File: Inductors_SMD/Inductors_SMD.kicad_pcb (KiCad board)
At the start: 2 copper layers, 11 parts

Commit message: Added new library with SMD inductors, mostly from Murata plus one of the most widespread sizes CDxx and DRxx.
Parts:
- removed CD104: VAL**, Inductors_SMD:CD104
- removed CD105: VAL**, Inductors_SMD:CD105
- removed CD32: VAL**, Inductors_SMD:CD32
- removed CD43: VAL**, Inductors_SMD:CD43
- removed CD54: VAL**, Inductors_SMD:CD54
- removed CD73: VAL**, Inductors_SMD:CD73
- removed CD75: VAL**, Inductors_SMD:CD75
- removed DR125: VAL**, Inductors_SMD:DR125
- removed DR127: VAL**, Inductors_SMD:DR127
- removed DR73: VAL**, Inductors_SMD:DR73
- removed DR74: VAL**, Inductors_SMD:DR74
- added REF**: CD104, CD104, F.Cu at (20.0, 20.0)
- added REF**: DR73, DR73, F.Cu at (34.0, 110.0)
- added REF**: LQM31P_Reflow, LQM31P, F.Cu at (132.0, 190.0)
- added REF**: LQM32P_Hand, LQM32P, F.Cu at (216.0, 20.0)
- added REF**: LQM32P_Reflow, LQM32P, F.Cu at (188.0, 20.0)
- added REF**: LQP02TN_Hand, LQP02TN, F.Cu at (216.0, 30.0)
- added REF**: LQP02TN_Reflow, LQP02TN, F.Cu at (188.0, 30.0)
- added REF**: LQP02TQ_Hand, LQP02TQ, F.Cu at (216.0, 40.0)
- added REF**: LQP02TQ_Reflow, LQP02TQ, F.Cu at (188.0, 40.0)
- added REF**: LQP03T_Hand, LQP03T, F.Cu at (216.0, 50.0)
- added REF**: LQP03T_Reflow, LQP03T, F.Cu at (188.0, 50.0)
- added REF**: LQP15M_Hand, LQP15M, F.Cu at (216.0, 60.0)
- added REF**: DR74, DR74, F.Cu at (20.0, 120.0)
- added REF**: LQP15M_Reflow, LQP15M, F.Cu at (188.0, 60.0)
- added REF**: LQP18M_Hand, LQP18M, F.Cu at (216.0, 70.0)
- added REF**: LQP18M_Reflow, LQP18M, F.Cu at (188.0, 70.0)
- added REF**: LQW03A_Hand, LQW03A, F.Cu at (216.0, 80.0)
- added REF**: LQW03A_Reflow, LQW03A, F.Cu at (188.0, 80.0)
- added REF**: LQW04A_Hand, LQW04A, F.Cu at (216.0, 90.0)
- added REF**: LQW04A_Reflow, LQW04A, F.Cu at (188.0, 90.0)
- added REF**: LQW15A_00_Hand, LQW15A_00, F.Cu at (216.0, 100.0)
- added REF**: LQW15A_00_Reflow, LQW15A_00, F.Cu at (188.0, 100.0)
- added REF**: LQW15A_80_Hand, LQW15A_80, F.Cu at (216.0, 110.0)
- added REF**: LQB15NN_Hand, LQB15NN, F.Cu at (48.0, 130.0)
- added REF**: LQW15A_80_Reflow, LQW15A_80, F.Cu at (188.0, 110.0)
- added REF**: LQW15C_00_Hand, LQW15C_00, F.Cu at (216.0, 120.0)
- added REF**: LQW15C_00_Reflow, LQW15C_00, F.Cu at (188.0, 120.0)
- added REF**: LQW15C_10_Hand, LQW15C_10, F.Cu at (216.0, 130.0)
- added REF**: LQW15C_10_Reflow, LQW15C_10, F.Cu at (188.0, 130.0)
- added REF**: LQW18A_00_Hand, LQW18A_00, F.Cu at (216.0, 140.0)
- added REF**: LQW18A_00_Reflow, LQW18A_00, F.Cu at (188.0, 140.0)
- added REF**: LQW18A_80_Hand, LQW18A_80, F.Cu at (216.0, 150.0)
- added REF**: LQW18A_80_Reflow, LQW18A_80, F.Cu at (188.0, 150.0)
- added REF**: LQW18C_Hand, LQW18C, F.Cu at (216.0, 160.0)
- added REF**: LQB15NN_Reflow, LQB15NN, F.Cu at (20.0, 130.0)
- added REF**: LQW18C_Reflow, LQW18C, F.Cu at (188.0, 160.0)
- added REF**: LQW21H_Hand, LQW21H, F.Cu at (216.0, 170.0)
- added REF**: LQW21H_Reflow, LQW21H, F.Cu at (188.0, 170.0)
- added REF**: LQW2BA_Hand, LQW2BA, F.Cu at (216.0, 180.0)
- added REF**: LQW2BA_Reflow, LQW2BA, F.Cu at (188.0, 180.0)
- added REF**: LQW2BH_Hand, LQW2BH, F.Cu at (216.0, 190.0)
- added REF**: LQW2BH_Reflow, LQW2BH, F.Cu at (188.0, 190.0)
- added REF**: LQW2UA_Hand, LQW2UA, F.Cu at (272.0, 20.0)
- added REF**: LQW2UA_Reflow, LQW2UA, F.Cu at (244.0, 20.0)
- added REF**: LQW31H_Hand, LQW31H, F.Cu at (272.0, 30.0)
- added REF**: LQB18N_Flow, LQB18N, F.Cu at (34.0, 140.0)
- added REF**: LQW31H_Reflow, LQW31H, F.Cu at (244.0, 30.0)
- added REF**: LQB18N_Hand, LQB18N, F.Cu at (48.0, 140.0)
- added REF**: LQB18N_Reflow, LQB18N, F.Cu at (20.0, 140.0)
- added REF**: LQG15H_Hand, LQG15H, F.Cu at (48.0, 150.0)
- added REF**: LQG15H_Reflow, LQG15H, F.Cu at (20.0, 150.0)
- added REF**: LQG18H_Hand, LQG18H, F.Cu at (48.0, 160.0)
- added REF**: CD105, CD105, F.Cu at (34.0, 30.0)
- added REF**: LQG18H_Reflow, LQG18H, F.Cu at (20.0, 160.0)
- added REF**: LQH2HP_GR_Hand, LQH2HP_GR, F.Cu at (48.0, 170.0)
- added REF**: LQH2HP_GR_Reflow, LQH2HP_GR, F.Cu at (20.0, 170.0)
- added REF**: LQH2HP_Hand, LQH2HP, F.Cu at (48.0, 180.0)
- added REF**: LQH2HP_Reflow, LQH2HP, F.Cu at (20.0, 180.0)
- added REF**: LQH2MC_Hand, LQH2MC, F.Cu at (48.0, 190.0)
- added REF**: LQH2MC_Reflow, LQH2MC, F.Cu at (20.0, 190.0)
- added REF**: LQH31C_Hand, LQH31C, F.Cu at (104.0, 20.0)
- added REF**: LQH31C_Reflow, LQH31C, F.Cu at (76.0, 20.0)
- added REF**: LQH31H_Hand, LQH31H, F.Cu at (104.0, 30.0)
- added REF**: CD32, CD32, F.Cu at (20.0, 40.0)
- added REF**: LQH31H_Reflow, LQH31H, F.Cu at (76.0, 30.0)
- added REF**: LQH31M_Hand, LQH31M, F.Cu at (104.0, 40.0)
- added REF**: LQH31M_Reflow, LQH31M, F.Cu at (76.0, 40.0)
- added REF**: LQH32C_Hand, LQH32C, F.Cu at (104.0, 50.0)
- added REF**: LQH32C_Reflow, LQH32C, F.Cu at (76.0, 50.0)
- added REF**: LQH32M_Hand, LQH32M, F.Cu at (104.0, 60.0)
- added REF**: LQH32M_Reflow, LQH32M, F.Cu at (76.0, 60.0)
- added REF**: LQH32P_Hand, LQH32P, F.Cu at (104.0, 70.0)
- added REF**: LQH32P_Reflow, LQH32P, F.Cu at (76.0, 70.0)
- added REF**: LQH3N_Hand, LQH3N, F.Cu at (104.0, 80.0)
- added REF**: CD43, CD43, F.Cu at (34.0, 50.0)
- added REF**: LQH3N_Reflow, LQH3N, F.Cu at (76.0, 80.0)
- added REF**: LQH43C_Hand, LQH43C, F.Cu at (104.0, 90.0)
- added REF**: LQH43C_Reflow, LQH43C, F.Cu at (76.0, 90.0)
- added REF**: LQH43M_Hand, LQH43M, F.Cu at (104.0, 100.0)
- added REF**: LQH43M_Reflow, LQH43M, F.Cu at (76.0, 100.0)
- added REF**: LQH43N_Hand, LQH43N, F.Cu at (104.0, 110.0)
- added REF**: LQH43N_Reflow, LQH43N, F.Cu at (76.0, 110.0)
- added REF**: LQH43P_Hand, LQH43P, F.Cu at (104.0, 120.0)
- added REF**: LQH43P_Reflow, LQH43P, F.Cu at (76.0, 120.0)
- added REF**: LQH44N_Hand, LQH44N, F.Cu at (104.0, 130.0)
- added REF**: CD54, CD54, F.Cu at (20.0, 60.0)
- added REF**: LQH44N_Reflow, LQH44N, F.Cu at (76.0, 130.0)
- added REF**: LQH44P_Hand, LQH44P, F.Cu at (104.0, 140.0)
- added REF**: LQH44P_Reflow, LQH44P, F.Cu at (76.0, 140.0)
- added REF**: LQH55D_Hand, LQH55D, F.Cu at (104.0, 150.0)
- added REF**: LQH55D_Reflow, LQH55D, F.Cu at (76.0, 150.0)
- added REF**: LQH5BP_Hand, LQH5BP, F.Cu at (104.0, 160.0)
- added REF**: LQH5BP_Reflow, LQH5BP, F.Cu at (76.0, 160.0)
- added REF**: LQH66S_Hand, LQH66S, F.Cu at (104.0, 170.0)
- added REF**: LQH66S_Reflow, LQH66S, F.Cu at (76.0, 170.0)
- added REF**: LQM18F_Flow, LQM18F, F.Cu at (90.0, 180.0)
- added REF**: CD73, CD73, F.Cu at (34.0, 70.0)
- added REF**: LQM18F_Hand, LQM18F, F.Cu at (104.0, 180.0)
- added REF**: LQM18F_Reflow, LQM18F, F.Cu at (76.0, 180.0)
- added REF**: LQM18N_Flow, LQM18N, F.Cu at (90.0, 190.0)
- added REF**: LQM18N_Hand, LQM18N, F.Cu at (104.0, 190.0)
- added REF**: LQM18N_Reflow, LQM18N, F.Cu at (76.0, 190.0)
- added REF**: LQM18P_Flow, LQM18P, F.Cu at (146.0, 20.0)
- added REF**: LQM18P_Hand, LQM18P, F.Cu at (160.0, 20.0)
- added REF**: LQM18P_Reflow, LQM18P, F.Cu at (132.0, 20.0)
- added REF**: LQM21D_Hand, LQM21D, F.Cu at (160.0, 30.0)
- added REF**: LQM21D_Reflow, LQM21D, F.Cu at (132.0, 30.0)
- added REF**: CD75, CD75, F.Cu at (20.0, 80.0)
- added REF**: LQM21F_Hand, LQM21F, F.Cu at (160.0, 40.0)
- added REF**: LQM21F_Reflow, LQM21F, F.Cu at (132.0, 40.0)
- added REF**: LQM21N_Flow, LQM21N, F.Cu at (146.0, 50.0)
- added REF**: LQM21N_Hand, LQM21N, F.Cu at (160.0, 50.0)
- added REF**: LQM21N_Reflow, LQM21N, F.Cu at (132.0, 50.0)
- added REF**: LQM21P_Hand, LQM21P, F.Cu at (160.0, 60.0)
- added REF**: LQM21P_Reflow, LQM21P, F.Cu at (132.0, 60.0)
- added REF**: LQM2HP_GH_1.5A_Hand, LQM2HP_GH_1.5A, F.Cu at (160.0, 70.0)
- added REF**: LQM2HP_GH_1.5A_Reflow, LQM2HP_GH_1.5A, F.Cu at (132.0, 70.0)
- added REF**: LQM2HP_GH_2.6A_Hand, LQM2HP_GH_2.6A, F.Cu at (160.0, 80.0)
- added REF**: DR125, DR125, F.Cu at (34.0, 90.0)
- added REF**: LQM2HP_GH_2.6A_Reflow, LQM2HP_GH_2.6A, F.Cu at (132.0, 80.0)
- added REF**: LQM2HP_GH_3.3A_Hand, LQM2HP_GH_3.3A, F.Cu at (160.0, 90.0)
- added REF**: LQM2HP_GH_3.3A_Reflow, LQM2HP_GH_3.3A, F.Cu at (132.0, 90.0)
- added REF**: LQM2HP_Hand, LQM2HP, F.Cu at (160.0, 100.0)
- added REF**: LQM2HP_JH_1.6A_Hand, LQM2HP_JH_1.6A, F.Cu at (160.0, 110.0)
- added REF**: LQM2HP_JH_1.6A_Reflow, LQM2HP_JH_1.6A, F.Cu at (132.0, 110.0)
- added REF**: LQM2HP_JH_2.4A_Hand, LQM2HP_JH_2.4A, F.Cu at (160.0, 120.0)
- added REF**: LQM2HP_JH_2.4A_Reflow, LQM2HP_JH_2.4A, F.Cu at (132.0, 120.0)
- added REF**: LQM2HP_JH_3.5A_Hand, LQM2HP_JH_3.5A, F.Cu at (160.0, 130.0)
- added REF**: LQM2HP_JH_3.5A_Reflow, LQM2HP_JH_3.5A, F.Cu at (132.0, 130.0)
- added REF**: DR127, DR127, F.Cu at (20.0, 100.0)
- added REF**: LQM2HP_Reflow, LQM2HP, F.Cu at (132.0, 140.0)
- added REF**: LQM2MP_GH_1.5A_Hand, LQM2MP_GH_1.5A, F.Cu at (160.0, 150.0)
- added REF**: LQM2MP_GH_1.5A_Reflow, LQM2MP_GH_1.5A, F.Cu at (132.0, 150.0)
- added REF**: LQM2MP_GH_2.5A_Hand, LQM2MP_GH_2.5A, F.Cu at (160.0, 160.0)
- added REF**: LQM2MP_GH_2.5A_Reflow, LQM2MP_GH_2.5A, F.Cu at (132.0, 160.0)
- added REF**: LQM2MP_GH_5A_Hand, LQM2MP_GH_5A, F.Cu at (160.0, 170.0)
- added REF**: LQM2MP_GH_5A_Reflow, LQM2MP_GH_5A, F.Cu at (132.0, 170.0)
- added REF**: LQM2MP_Hand, LQM2MP, F.Cu at (160.0, 180.0)
- added REF**: LQM2MP_Reflow, LQM2MP, F.Cu at (132.0, 180.0)
- added REF**: LQM31P_Hand, LQM31P, F.Cu at (160.0, 190.0)
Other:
- net class Default: clearance 0.254 -> 0.25; trace_width 0.254 -> 0.25; via_dia 0.889 -> 0.6; via_drill 0.635 -> 0.4
- rule trace_clearance: 0.254 -> 0.25
- rule trace_min: 0.254 -> 0.2
- rule via_min_drill: 0.508 -> 0.3
- rule via_min_size: 0.889 -> 0.4

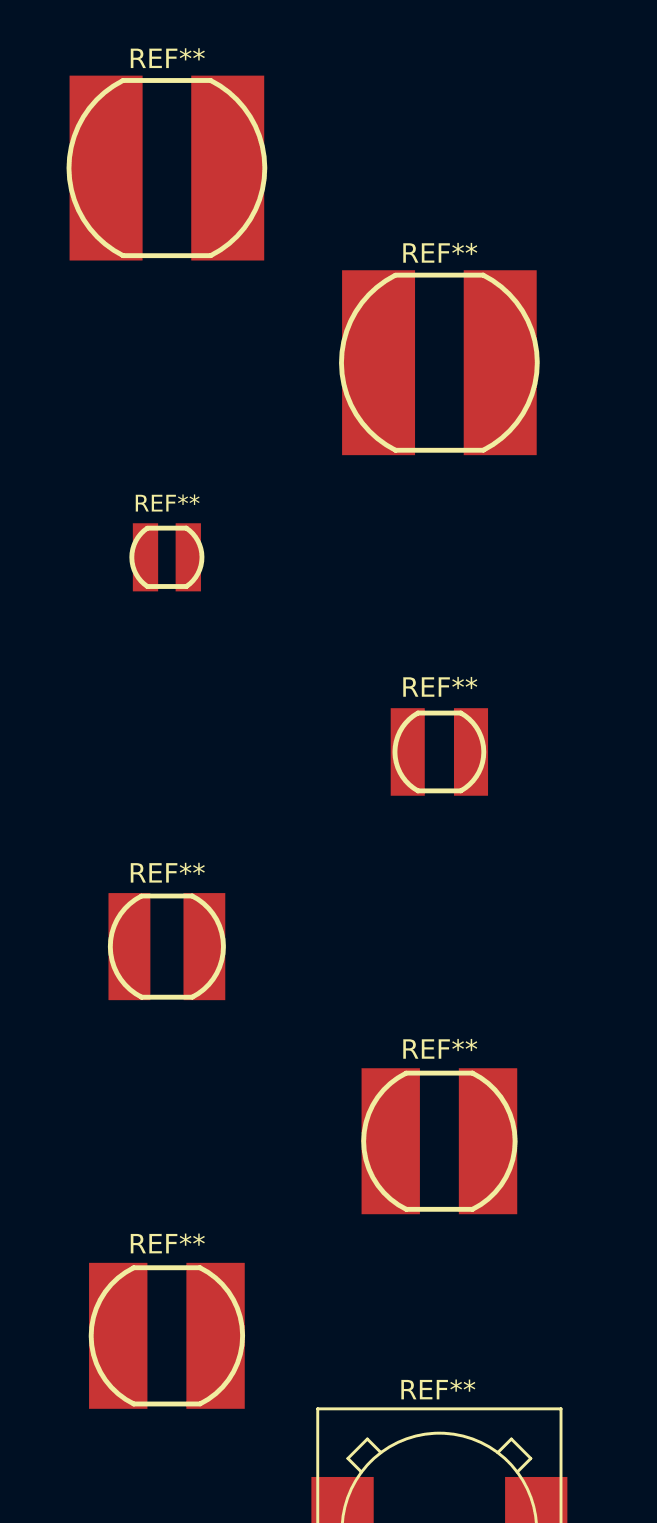
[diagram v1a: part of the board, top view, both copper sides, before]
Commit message: * Added Blender files to repository. * Fixed component generation scripts to avoid breaking some KLC rules
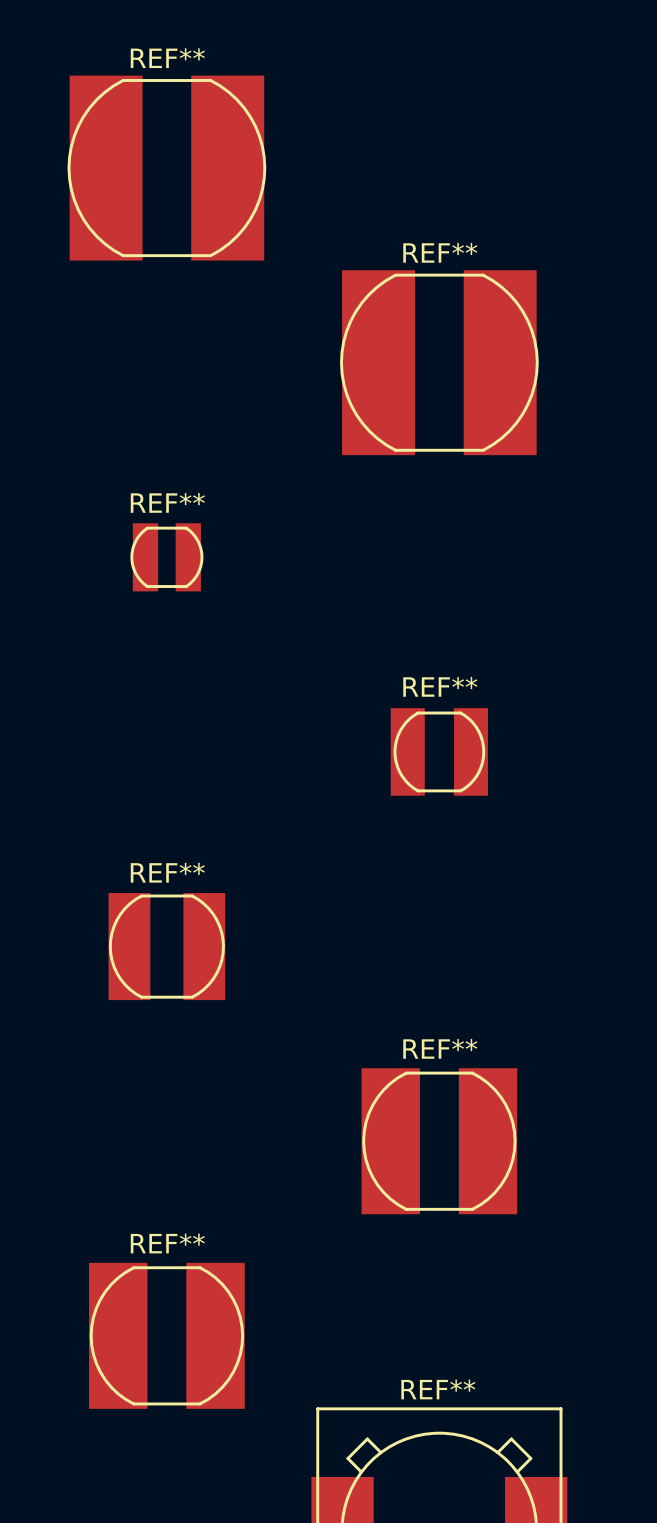
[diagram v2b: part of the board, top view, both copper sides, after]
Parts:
- removed the REF** at (132.0, 190.0)
- removed the REF** at (216.0, 20.0)
- removed the REF** at (188.0, 20.0)
- removed the REF** at (216.0, 30.0)
- removed the REF** at (188.0, 30.0)
- removed the REF** at (216.0, 40.0)
- removed the REF** at (188.0, 40.0)
- removed the REF** at (216.0, 50.0)
- removed the REF** at (188.0, 50.0)
- removed the REF** at (216.0, 60.0)
- removed the REF** at (188.0, 60.0)
- removed the REF** at (216.0, 70.0)
- removed the REF** at (188.0, 70.0)
- removed the REF** at (216.0, 80.0)
- removed the REF** at (188.0, 80.0)
- removed the REF** at (216.0, 90.0)
- removed the REF** at (188.0, 90.0)
- removed the REF** at (216.0, 100.0)
- removed the REF** at (188.0, 100.0)
- removed the REF** at (216.0, 110.0)
- removed the REF** at (48.0, 130.0)
- removed the REF** at (188.0, 110.0)
- removed the REF** at (216.0, 120.0)
- removed the REF** at (188.0, 120.0)
- removed the REF** at (216.0, 130.0)
- removed the REF** at (188.0, 130.0)
- removed the REF** at (216.0, 140.0)
- removed the REF** at (188.0, 140.0)
- removed the REF** at (216.0, 150.0)
- removed the REF** at (188.0, 150.0)
- removed the REF** at (216.0, 160.0)
- removed the REF** at (20.0, 130.0)
- removed the REF** at (188.0, 160.0)
- removed the REF** at (216.0, 170.0)
- removed the REF** at (188.0, 170.0)
- removed the REF** at (216.0, 180.0)
- removed the REF** at (188.0, 180.0)
- removed the REF** at (216.0, 190.0)
- removed the REF** at (188.0, 190.0)
- removed the REF** at (272.0, 20.0)
- removed the REF** at (244.0, 20.0)
- removed the REF** at (272.0, 30.0)
- removed the REF** at (34.0, 140.0)
- removed the REF** at (244.0, 30.0)
- removed the REF** at (48.0, 140.0)
- removed the REF** at (20.0, 140.0)
- removed the REF** at (48.0, 150.0)
- removed the REF** at (20.0, 150.0)
- removed the REF** at (48.0, 160.0)
- removed the REF** at (20.0, 160.0)
- removed the REF** at (48.0, 170.0)
- removed the REF** at (20.0, 170.0)
- removed the REF** at (48.0, 180.0)
- removed the REF** at (20.0, 180.0)
- removed the REF** at (48.0, 190.0)
- removed the REF** at (20.0, 190.0)
- removed the REF** at (104.0, 20.0)
- removed the REF** at (76.0, 20.0)
- removed the REF** at (104.0, 30.0)
- removed the REF** at (76.0, 30.0)
- removed the REF** at (104.0, 40.0)
- removed the REF** at (76.0, 40.0)
- removed the REF** at (104.0, 50.0)
- removed the REF** at (76.0, 50.0)
- removed the REF** at (104.0, 60.0)
- removed the REF** at (76.0, 60.0)
- removed the REF** at (104.0, 70.0)
- removed the REF** at (76.0, 70.0)
- removed the REF** at (104.0, 80.0)
- removed the REF** at (76.0, 80.0)
- removed the REF** at (104.0, 90.0)
- removed the REF** at (76.0, 90.0)
- removed the REF** at (104.0, 100.0)
- removed the REF** at (76.0, 100.0)
- removed the REF** at (104.0, 110.0)
- removed the REF** at (76.0, 110.0)
- removed the REF** at (104.0, 120.0)
- removed the REF** at (76.0, 120.0)
- removed the REF** at (104.0, 130.0)
- removed the REF** at (76.0, 130.0)
- removed the REF** at (104.0, 140.0)
- removed the REF** at (76.0, 140.0)
- removed the REF** at (104.0, 150.0)
- removed the REF** at (76.0, 150.0)
- removed the REF** at (104.0, 160.0)
- removed the REF** at (76.0, 160.0)
- removed the REF** at (104.0, 170.0)
- removed the REF** at (76.0, 170.0)
- removed the REF** at (90.0, 180.0)
- removed the REF** at (104.0, 180.0)
- removed the REF** at (76.0, 180.0)
- removed the REF** at (90.0, 190.0)
- removed the REF** at (104.0, 190.0)
- removed the REF** at (76.0, 190.0)
- removed the REF** at (146.0, 20.0)
- removed the REF** at (160.0, 20.0)
- removed the REF** at (132.0, 20.0)
- removed the REF** at (160.0, 30.0)
- removed the REF** at (132.0, 30.0)
- removed the REF** at (160.0, 40.0)
- removed the REF** at (132.0, 40.0)
- removed the REF** at (146.0, 50.0)
- removed the REF** at (160.0, 50.0)
- removed the REF** at (132.0, 50.0)
- removed the REF** at (160.0, 60.0)
- removed the REF** at (132.0, 60.0)
- removed the REF** at (160.0, 70.0)
- removed the REF** at (132.0, 70.0)
- removed the REF** at (160.0, 80.0)
- removed the REF** at (132.0, 80.0)
- removed the REF** at (160.0, 90.0)
- removed the REF** at (132.0, 90.0)
- removed the REF** at (160.0, 100.0)
- removed the REF** at (160.0, 110.0)
- removed the REF** at (132.0, 110.0)
- removed the REF** at (160.0, 120.0)
- removed the REF** at (132.0, 120.0)
- removed the REF** at (160.0, 130.0)
- removed the REF** at (132.0, 130.0)
- removed the REF** at (132.0, 140.0)
- removed the REF** at (160.0, 150.0)
- removed the REF** at (132.0, 150.0)
- removed the REF** at (160.0, 160.0)
- removed the REF** at (132.0, 160.0)
- removed the REF** at (160.0, 170.0)
- removed the REF** at (132.0, 170.0)
- removed the REF** at (160.0, 180.0)
- removed the REF** at (132.0, 180.0)
- removed the REF** at (160.0, 190.0)
- added REF**: LQM31P_Reflow, LQM31P_Reflow, F.Cu at (132.0, 190.0)
- added REF**: LQM32P_Hand, LQM32P_Hand, F.Cu at (216.0, 20.0)
- added REF**: LQM32P_Reflow, LQM32P_Reflow, F.Cu at (188.0, 20.0)
- added REF**: LQP02TN_Hand, LQP02TN_Hand, F.Cu at (216.0, 30.0)
- added REF**: LQP02TN_Reflow, LQP02TN_Reflow, F.Cu at (188.0, 30.0)
- added REF**: LQP02TQ_Hand, LQP02TQ_Hand, F.Cu at (216.0, 40.0)
- added REF**: LQP02TQ_Reflow, LQP02TQ_Reflow, F.Cu at (188.0, 40.0)
- added REF**: LQP03T_Hand, LQP03T_Hand, F.Cu at (216.0, 50.0)
- added REF**: LQP03T_Reflow, LQP03T_Reflow, F.Cu at (188.0, 50.0)
- added REF**: LQP15M_Hand, LQP15M_Hand, F.Cu at (216.0, 60.0)
- added REF**: LQP15M_Reflow, LQP15M_Reflow, F.Cu at (188.0, 60.0)
- added REF**: LQP18M_Hand, LQP18M_Hand, F.Cu at (216.0, 70.0)
- added REF**: LQP18M_Reflow, LQP18M_Reflow, F.Cu at (188.0, 70.0)
- added REF**: LQW03A_Hand, LQW03A_Hand, F.Cu at (216.0, 80.0)
- added REF**: LQW03A_Reflow, LQW03A_Reflow, F.Cu at (188.0, 80.0)
- added REF**: LQW04A_Hand, LQW04A_Hand, F.Cu at (216.0, 90.0)
- added REF**: LQW04A_Reflow, LQW04A_Reflow, F.Cu at (188.0, 90.0)
- added REF**: LQW15A_00_Hand, LQW15A_00_Hand, F.Cu at (216.0, 100.0)
- added REF**: LQW15A_00_Reflow, LQW15A_00_Reflow, F.Cu at (188.0, 100.0)
- added REF**: LQW15A_80_Hand, LQW15A_80_Hand, F.Cu at (216.0, 110.0)
- added REF**: LQB15NN_Hand, LQB15NN_Hand, F.Cu at (48.0, 130.0)
- added REF**: LQW15A_80_Reflow, LQW15A_80_Reflow, F.Cu at (188.0, 110.0)
- added REF**: LQW15C_00_Hand, LQW15C_00_Hand, F.Cu at (216.0, 120.0)
- added REF**: LQW15C_00_Reflow, LQW15C_00_Reflow, F.Cu at (188.0, 120.0)
- added REF**: LQW15C_10_Hand, LQW15C_10_Hand, F.Cu at (216.0, 130.0)
- added REF**: LQW15C_10_Reflow, LQW15C_10_Reflow, F.Cu at (188.0, 130.0)
- added REF**: LQW18A_00_Hand, LQW18A_00_Hand, F.Cu at (216.0, 140.0)
- added REF**: LQW18A_00_Reflow, LQW18A_00_Reflow, F.Cu at (188.0, 140.0)
- added REF**: LQW18A_80_Hand, LQW18A_80_Hand, F.Cu at (216.0, 150.0)
- added REF**: LQW18A_80_Reflow, LQW18A_80_Reflow, F.Cu at (188.0, 150.0)
- added REF**: LQW18C_Hand, LQW18C_Hand, F.Cu at (216.0, 160.0)
- added REF**: LQB15NN_Reflow, LQB15NN_Reflow, F.Cu at (20.0, 130.0)
- added REF**: LQW18C_Reflow, LQW18C_Reflow, F.Cu at (188.0, 160.0)
- added REF**: LQW21H_Hand, LQW21H_Hand, F.Cu at (216.0, 170.0)
- added REF**: LQW21H_Reflow, LQW21H_Reflow, F.Cu at (188.0, 170.0)
- added REF**: LQW2BA_Hand, LQW2BA_Hand, F.Cu at (216.0, 180.0)
- added REF**: LQW2BA_Reflow, LQW2BA_Reflow, F.Cu at (188.0, 180.0)
- added REF**: LQW2BH_Hand, LQW2BH_Hand, F.Cu at (216.0, 190.0)
- added REF**: LQW2BH_Reflow, LQW2BH_Reflow, F.Cu at (188.0, 190.0)
- added REF**: LQW2UA_Hand, LQW2UA_Hand, F.Cu at (272.0, 20.0)
- added REF**: LQW2UA_Reflow, LQW2UA_Reflow, F.Cu at (244.0, 20.0)
- added REF**: LQW31H_Hand, LQW31H_Hand, F.Cu at (272.0, 30.0)
- added REF**: LQB18N_Flow, LQB18N_Flow, F.Cu at (34.0, 140.0)
- added REF**: LQW31H_Reflow, LQW31H_Reflow, F.Cu at (244.0, 30.0)
- added REF**: LQB18N_Hand, LQB18N_Hand, F.Cu at (48.0, 140.0)
- added REF**: LQB18N_Reflow, LQB18N_Reflow, F.Cu at (20.0, 140.0)
- added REF**: LQG15H_Hand, LQG15H_Hand, F.Cu at (48.0, 150.0)
- added REF**: LQG15H_Reflow, LQG15H_Reflow, F.Cu at (20.0, 150.0)
- added REF**: LQG18H_Hand, LQG18H_Hand, F.Cu at (48.0, 160.0)
- added REF**: LQG18H_Reflow, LQG18H_Reflow, F.Cu at (20.0, 160.0)
- added REF**: LQH2HP_GR_Hand, LQH2HP_GR_Hand, F.Cu at (48.0, 170.0)
- added REF**: LQH2HP_GR_Reflow, LQH2HP_GR_Reflow, F.Cu at (20.0, 170.0)
- added REF**: LQH2HP_Hand, LQH2HP_Hand, F.Cu at (48.0, 180.0)
- added REF**: LQH2HP_Reflow, LQH2HP_Reflow, F.Cu at (20.0, 180.0)
- added REF**: LQH2MC_Hand, LQH2MC_Hand, F.Cu at (48.0, 190.0)
- added REF**: LQH2MC_Reflow, LQH2MC_Reflow, F.Cu at (20.0, 190.0)
- added REF**: LQH31C_Hand, LQH31C_Hand, F.Cu at (104.0, 20.0)
- added REF**: LQH31C_Reflow, LQH31C_Reflow, F.Cu at (76.0, 20.0)
- added REF**: LQH31H_Hand, LQH31H_Hand, F.Cu at (104.0, 30.0)
- added REF**: LQH31H_Reflow, LQH31H_Reflow, F.Cu at (76.0, 30.0)
- added REF**: LQH31M_Hand, LQH31M_Hand, F.Cu at (104.0, 40.0)
- added REF**: LQH31M_Reflow, LQH31M_Reflow, F.Cu at (76.0, 40.0)
- added REF**: LQH32C_Hand, LQH32C_Hand, F.Cu at (104.0, 50.0)
- added REF**: LQH32C_Reflow, LQH32C_Reflow, F.Cu at (76.0, 50.0)
- added REF**: LQH32M_Hand, LQH32M_Hand, F.Cu at (104.0, 60.0)
- added REF**: LQH32M_Reflow, LQH32M_Reflow, F.Cu at (76.0, 60.0)
- added REF**: LQH32P_Hand, LQH32P_Hand, F.Cu at (104.0, 70.0)
- added REF**: LQH32P_Reflow, LQH32P_Reflow, F.Cu at (76.0, 70.0)
- added REF**: LQH3N_Hand, LQH3N_Hand, F.Cu at (104.0, 80.0)
- added REF**: LQH3N_Reflow, LQH3N_Reflow, F.Cu at (76.0, 80.0)
- added REF**: LQH43C_Hand, LQH43C_Hand, F.Cu at (104.0, 90.0)
- added REF**: LQH43C_Reflow, LQH43C_Reflow, F.Cu at (76.0, 90.0)
- added REF**: LQH43M_Hand, LQH43M_Hand, F.Cu at (104.0, 100.0)
- added REF**: LQH43M_Reflow, LQH43M_Reflow, F.Cu at (76.0, 100.0)
- added REF**: LQH43N_Hand, LQH43N_Hand, F.Cu at (104.0, 110.0)
- added REF**: LQH43N_Reflow, LQH43N_Reflow, F.Cu at (76.0, 110.0)
- added REF**: LQH43P_Hand, LQH43P_Hand, F.Cu at (104.0, 120.0)
- added REF**: LQH43P_Reflow, LQH43P_Reflow, F.Cu at (76.0, 120.0)
- added REF**: LQH44N_Hand, LQH44N_Hand, F.Cu at (104.0, 130.0)
- added REF**: LQH44N_Reflow, LQH44N_Reflow, F.Cu at (76.0, 130.0)
- added REF**: LQH44P_Hand, LQH44P_Hand, F.Cu at (104.0, 140.0)
- added REF**: LQH44P_Reflow, LQH44P_Reflow, F.Cu at (76.0, 140.0)
- added REF**: LQH55D_Hand, LQH55D_Hand, F.Cu at (104.0, 150.0)
- added REF**: LQH55D_Reflow, LQH55D_Reflow, F.Cu at (76.0, 150.0)
- added REF**: LQH5BP_Hand, LQH5BP_Hand, F.Cu at (104.0, 160.0)
- added REF**: LQH5BP_Reflow, LQH5BP_Reflow, F.Cu at (76.0, 160.0)
- added REF**: LQH66S_Hand, LQH66S_Hand, F.Cu at (104.0, 170.0)
- added REF**: LQH66S_Reflow, LQH66S_Reflow, F.Cu at (76.0, 170.0)
- added REF**: LQM18F_Flow, LQM18F_Flow, F.Cu at (90.0, 180.0)
- added REF**: LQM18F_Hand, LQM18F_Hand, F.Cu at (104.0, 180.0)
- added REF**: LQM18F_Reflow, LQM18F_Reflow, F.Cu at (76.0, 180.0)
- added REF**: LQM18N_Flow, LQM18N_Flow, F.Cu at (90.0, 190.0)
- added REF**: LQM18N_Hand, LQM18N_Hand, F.Cu at (104.0, 190.0)
- added REF**: LQM18N_Reflow, LQM18N_Reflow, F.Cu at (76.0, 190.0)
- added REF**: LQM18P_Flow, LQM18P_Flow, F.Cu at (146.0, 20.0)
- added REF**: LQM18P_Hand, LQM18P_Hand, F.Cu at (160.0, 20.0)
- added REF**: LQM18P_Reflow, LQM18P_Reflow, F.Cu at (132.0, 20.0)
- added REF**: LQM21D_Hand, LQM21D_Hand, F.Cu at (160.0, 30.0)
- added REF**: LQM21D_Reflow, LQM21D_Reflow, F.Cu at (132.0, 30.0)
- added REF**: LQM21F_Hand, LQM21F_Hand, F.Cu at (160.0, 40.0)
- added REF**: LQM21F_Reflow, LQM21F_Reflow, F.Cu at (132.0, 40.0)
- added REF**: LQM21N_Flow, LQM21N_Flow, F.Cu at (146.0, 50.0)
- added REF**: LQM21N_Hand, LQM21N_Hand, F.Cu at (160.0, 50.0)
- added REF**: LQM21N_Reflow, LQM21N_Reflow, F.Cu at (132.0, 50.0)
- added REF**: LQM21P_Hand, LQM21P_Hand, F.Cu at (160.0, 60.0)
- added REF**: LQM21P_Reflow, LQM21P_Reflow, F.Cu at (132.0, 60.0)
- added REF**: LQM2HP_GH_1.5A_Hand, LQM2HP_GH_1.5A_Hand, F.Cu at (160.0, 70.0)
- added REF**: LQM2HP_GH_1.5A_Reflow, LQM2HP_GH_1.5A_Reflow, F.Cu at (132.0, 70.0)
- added REF**: LQM2HP_GH_2.6A_Hand, LQM2HP_GH_2.6A_Hand, F.Cu at (160.0, 80.0)
- added REF**: LQM2HP_GH_2.6A_Reflow, LQM2HP_GH_2.6A_Reflow, F.Cu at (132.0, 80.0)
- added REF**: LQM2HP_GH_3.3A_Hand, LQM2HP_GH_3.3A_Hand, F.Cu at (160.0, 90.0)
- added REF**: LQM2HP_GH_3.3A_Reflow, LQM2HP_GH_3.3A_Reflow, F.Cu at (132.0, 90.0)
- added REF**: LQM2HP_Hand, LQM2HP_Hand, F.Cu at (160.0, 100.0)
- added REF**: LQM2HP_JH_1.6A_Hand, LQM2HP_JH_1.6A_Hand, F.Cu at (160.0, 110.0)
- added REF**: LQM2HP_JH_1.6A_Reflow, LQM2HP_JH_1.6A_Reflow, F.Cu at (132.0, 110.0)
- added REF**: LQM2HP_JH_2.4A_Hand, LQM2HP_JH_2.4A_Hand, F.Cu at (160.0, 120.0)
- added REF**: LQM2HP_JH_2.4A_Reflow, LQM2HP_JH_2.4A_Reflow, F.Cu at (132.0, 120.0)
- added REF**: LQM2HP_JH_3.5A_Hand, LQM2HP_JH_3.5A_Hand, F.Cu at (160.0, 130.0)
- added REF**: LQM2HP_JH_3.5A_Reflow, LQM2HP_JH_3.5A_Reflow, F.Cu at (132.0, 130.0)
- added REF**: LQM2HP_Reflow, LQM2HP_Reflow, F.Cu at (132.0, 140.0)
- added REF**: LQM2MP_GH_1.5A_Hand, LQM2MP_GH_1.5A_Hand, F.Cu at (160.0, 150.0)
- added REF**: LQM2MP_GH_1.5A_Reflow, LQM2MP_GH_1.5A_Reflow, F.Cu at (132.0, 150.0)
- added REF**: LQM2MP_GH_2.5A_Hand, LQM2MP_GH_2.5A_Hand, F.Cu at (160.0, 160.0)
- added REF**: LQM2MP_GH_2.5A_Reflow, LQM2MP_GH_2.5A_Reflow, F.Cu at (132.0, 160.0)
- added REF**: LQM2MP_GH_5A_Hand, LQM2MP_GH_5A_Hand, F.Cu at (160.0, 170.0)
- added REF**: LQM2MP_GH_5A_Reflow, LQM2MP_GH_5A_Reflow, F.Cu at (132.0, 170.0)
- added REF**: LQM2MP_Hand, LQM2MP_Hand, F.Cu at (160.0, 180.0)
- added REF**: LQM2MP_Reflow, LQM2MP_Reflow, F.Cu at (132.0, 180.0)
- added REF**: LQM31P_Hand, LQM31P_Hand, F.Cu at (160.0, 190.0)

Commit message: Renamed all inductors to Choke_XXX, both footprint and 3d model.
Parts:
- removed the REF** at (20.0, 20.0)
- removed the REF** at (34.0, 110.0)
- removed the REF** at (132.0, 190.0)
- removed the REF** at (216.0, 20.0)
- removed the REF** at (188.0, 20.0)
- removed the REF** at (216.0, 30.0)
- removed the REF** at (188.0, 30.0)
- removed the REF** at (216.0, 40.0)
- removed the REF** at (188.0, 40.0)
- removed the REF** at (216.0, 50.0)
- removed the REF** at (188.0, 50.0)
- removed the REF** at (216.0, 60.0)
- removed the REF** at (20.0, 120.0)
- removed the REF** at (188.0, 60.0)
- removed the REF** at (216.0, 70.0)
- removed the REF** at (188.0, 70.0)
- removed the REF** at (216.0, 80.0)
- removed the REF** at (188.0, 80.0)
- removed the REF** at (216.0, 90.0)
- removed the REF** at (188.0, 90.0)
- removed the REF** at (216.0, 100.0)
- removed the REF** at (188.0, 100.0)
- removed the REF** at (216.0, 110.0)
- removed the REF** at (48.0, 130.0)
- removed the REF** at (188.0, 110.0)
- removed the REF** at (216.0, 120.0)
- removed the REF** at (188.0, 120.0)
- removed the REF** at (216.0, 130.0)
- removed the REF** at (188.0, 130.0)
- removed the REF** at (216.0, 140.0)
- removed the REF** at (188.0, 140.0)
- removed the REF** at (216.0, 150.0)
- removed the REF** at (188.0, 150.0)
- removed the REF** at (216.0, 160.0)
- removed the REF** at (20.0, 130.0)
- removed the REF** at (188.0, 160.0)
- removed the REF** at (216.0, 170.0)
- removed the REF** at (188.0, 170.0)
- removed the REF** at (216.0, 180.0)
- removed the REF** at (188.0, 180.0)
- removed the REF** at (216.0, 190.0)
- removed the REF** at (188.0, 190.0)
- removed the REF** at (272.0, 20.0)
- removed the REF** at (244.0, 20.0)
- removed the REF** at (272.0, 30.0)
- removed the REF** at (34.0, 140.0)
- removed the REF** at (244.0, 30.0)
- removed the REF** at (48.0, 140.0)
- removed the REF** at (20.0, 140.0)
- removed the REF** at (48.0, 150.0)
- removed the REF** at (20.0, 150.0)
- removed the REF** at (48.0, 160.0)
- removed the REF** at (34.0, 30.0)
- removed the REF** at (20.0, 160.0)
- removed the REF** at (48.0, 170.0)
- removed the REF** at (20.0, 170.0)
- removed the REF** at (48.0, 180.0)
- removed the REF** at (20.0, 180.0)
- removed the REF** at (48.0, 190.0)
- removed the REF** at (20.0, 190.0)
- removed the REF** at (104.0, 20.0)
- removed the REF** at (76.0, 20.0)
- removed the REF** at (104.0, 30.0)
- removed the REF** at (20.0, 40.0)
- removed the REF** at (76.0, 30.0)
- removed the REF** at (104.0, 40.0)
- removed the REF** at (76.0, 40.0)
- removed the REF** at (104.0, 50.0)
- removed the REF** at (76.0, 50.0)
- removed the REF** at (104.0, 60.0)
- removed the REF** at (76.0, 60.0)
- removed the REF** at (104.0, 70.0)
- removed the REF** at (76.0, 70.0)
- removed the REF** at (104.0, 80.0)
- removed the REF** at (34.0, 50.0)
- removed the REF** at (76.0, 80.0)
- removed the REF** at (104.0, 90.0)
- removed the REF** at (76.0, 90.0)
- removed the REF** at (104.0, 100.0)
- removed the REF** at (76.0, 100.0)
- removed the REF** at (104.0, 110.0)
- removed the REF** at (76.0, 110.0)
- removed the REF** at (104.0, 120.0)
- removed the REF** at (76.0, 120.0)
- removed the REF** at (104.0, 130.0)
- removed the REF** at (20.0, 60.0)
- removed the REF** at (76.0, 130.0)
- removed the REF** at (104.0, 140.0)
- removed the REF** at (76.0, 140.0)
- removed the REF** at (104.0, 150.0)
- removed the REF** at (76.0, 150.0)
- removed the REF** at (104.0, 160.0)
- removed the REF** at (76.0, 160.0)
- removed the REF** at (104.0, 170.0)
- removed the REF** at (76.0, 170.0)
- removed the REF** at (90.0, 180.0)
- removed the REF** at (34.0, 70.0)
- removed the REF** at (104.0, 180.0)
- removed the REF** at (76.0, 180.0)
- removed the REF** at (90.0, 190.0)
- removed the REF** at (104.0, 190.0)
- removed the REF** at (76.0, 190.0)
- removed the REF** at (146.0, 20.0)
- removed the REF** at (160.0, 20.0)
- removed the REF** at (132.0, 20.0)
- removed the REF** at (160.0, 30.0)
- removed the REF** at (132.0, 30.0)
- removed the REF** at (20.0, 80.0)
- removed the REF** at (160.0, 40.0)
- removed the REF** at (132.0, 40.0)
- removed the REF** at (146.0, 50.0)
- removed the REF** at (160.0, 50.0)
- removed the REF** at (132.0, 50.0)
- removed the REF** at (160.0, 60.0)
- removed the REF** at (132.0, 60.0)
- removed the REF** at (160.0, 70.0)
- removed the REF** at (132.0, 70.0)
- removed the REF** at (160.0, 80.0)
- removed the REF** at (34.0, 90.0)
- removed the REF** at (132.0, 80.0)
- removed the REF** at (160.0, 90.0)
- removed the REF** at (132.0, 90.0)
- removed the REF** at (160.0, 100.0)
- removed the REF** at (160.0, 110.0)
- removed the REF** at (132.0, 110.0)
- removed the REF** at (160.0, 120.0)
- removed the REF** at (132.0, 120.0)
- removed the REF** at (160.0, 130.0)
- removed the REF** at (132.0, 130.0)
- removed the REF** at (20.0, 100.0)
- removed the REF** at (132.0, 140.0)
- removed the REF** at (160.0, 150.0)
- removed the REF** at (132.0, 150.0)
- removed the REF** at (160.0, 160.0)
- removed the REF** at (132.0, 160.0)
- removed the REF** at (160.0, 170.0)
- removed the REF** at (132.0, 170.0)
- removed the REF** at (160.0, 180.0)
- removed the REF** at (132.0, 180.0)
- removed the REF** at (160.0, 190.0)
- added REF**: CD104, Choke_CD104, F.Cu at (20.0, 20.0)
- added REF**: DR73, Choke_DR73, F.Cu at (34.0, 110.0)
- added REF**: Choke_LQM31P_Reflow, Choke_LQM31P_Reflow, F.Cu at (132.0, 190.0)
- added REF**: Choke_LQM32P_Hand, Choke_LQM32P_Hand, F.Cu at (216.0, 20.0)
- added REF**: Choke_LQM32P_Reflow, Choke_LQM32P_Reflow, F.Cu at (188.0, 20.0)
- added REF**: Choke_LQP02TN_Hand, Choke_LQP02TN_Hand, F.Cu at (216.0, 30.0)
- added REF**: Choke_LQP02TN_Reflow, Choke_LQP02TN_Reflow, F.Cu at (188.0, 30.0)
- added REF**: Choke_LQP02TQ_Hand, Choke_LQP02TQ_Hand, F.Cu at (216.0, 40.0)
- added REF**: Choke_LQP02TQ_Reflow, Choke_LQP02TQ_Reflow, F.Cu at (188.0, 40.0)
- added REF**: Choke_LQP03T_Hand, Choke_LQP03T_Hand, F.Cu at (216.0, 50.0)
- added REF**: Choke_LQP03T_Reflow, Choke_LQP03T_Reflow, F.Cu at (188.0, 50.0)
- added REF**: Choke_LQP15M_Hand, Choke_LQP15M_Hand, F.Cu at (216.0, 60.0)
- added REF**: DR74, Choke_DR74, F.Cu at (20.0, 120.0)
- added REF**: Choke_LQP15M_Reflow, Choke_LQP15M_Reflow, F.Cu at (188.0, 60.0)
- added REF**: Choke_LQP18M_Hand, Choke_LQP18M_Hand, F.Cu at (216.0, 70.0)
- added REF**: Choke_LQP18M_Reflow, Choke_LQP18M_Reflow, F.Cu at (188.0, 70.0)
- added REF**: Choke_LQW03A_Hand, Choke_LQW03A_Hand, F.Cu at (216.0, 80.0)
- added REF**: Choke_LQW03A_Reflow, Choke_LQW03A_Reflow, F.Cu at (188.0, 80.0)
- added REF**: Choke_LQW04A_Hand, Choke_LQW04A_Hand, F.Cu at (216.0, 90.0)
- added REF**: Choke_LQW04A_Reflow, Choke_LQW04A_Reflow, F.Cu at (188.0, 90.0)
- added REF**: Choke_LQW15A_00_Hand, Choke_LQW15A_00_Hand, F.Cu at (216.0, 100.0)
- added REF**: Choke_LQW15A_00_Reflow, Choke_LQW15A_00_Reflow, F.Cu at (188.0, 100.0)
- added REF**: Choke_LQW15A_80_Hand, Choke_LQW15A_80_Hand, F.Cu at (216.0, 110.0)
- added REF**: Choke_LQB15NN_Hand, Choke_LQB15NN_Hand, F.Cu at (48.0, 130.0)
- added REF**: Choke_LQW15A_80_Reflow, Choke_LQW15A_80_Reflow, F.Cu at (188.0, 110.0)
- added REF**: Choke_LQW15C_00_Hand, Choke_LQW15C_00_Hand, F.Cu at (216.0, 120.0)
- added REF**: Choke_LQW15C_00_Reflow, Choke_LQW15C_00_Reflow, F.Cu at (188.0, 120.0)
- added REF**: Choke_LQW15C_10_Hand, Choke_LQW15C_10_Hand, F.Cu at (216.0, 130.0)
- added REF**: Choke_LQW15C_10_Reflow, Choke_LQW15C_10_Reflow, F.Cu at (188.0, 130.0)
- added REF**: Choke_LQW18A_00_Hand, Choke_LQW18A_00_Hand, F.Cu at (216.0, 140.0)
- added REF**: Choke_LQW18A_00_Reflow, Choke_LQW18A_00_Reflow, F.Cu at (188.0, 140.0)
- added REF**: Choke_LQW18A_80_Hand, Choke_LQW18A_80_Hand, F.Cu at (216.0, 150.0)
- added REF**: Choke_LQW18A_80_Reflow, Choke_LQW18A_80_Reflow, F.Cu at (188.0, 150.0)
- added REF**: Choke_LQW18C_Hand, Choke_LQW18C_Hand, F.Cu at (216.0, 160.0)
- added REF**: Choke_LQB15NN_Reflow, Choke_LQB15NN_Reflow, F.Cu at (20.0, 130.0)
- added REF**: Choke_LQW18C_Reflow, Choke_LQW18C_Reflow, F.Cu at (188.0, 160.0)
- added REF**: Choke_LQW21H_Hand, Choke_LQW21H_Hand, F.Cu at (216.0, 170.0)
- added REF**: Choke_LQW21H_Reflow, Choke_LQW21H_Reflow, F.Cu at (188.0, 170.0)
- added REF**: Choke_LQW2BA_Hand, Choke_LQW2BA_Hand, F.Cu at (216.0, 180.0)
- added REF**: Choke_LQW2BA_Reflow, Choke_LQW2BA_Reflow, F.Cu at (188.0, 180.0)
- added REF**: Choke_LQW2BH_Hand, Choke_LQW2BH_Hand, F.Cu at (216.0, 190.0)
- added REF**: Choke_LQW2BH_Reflow, Choke_LQW2BH_Reflow, F.Cu at (188.0, 190.0)
- added REF**: Choke_LQW2UA_Hand, Choke_LQW2UA_Hand, F.Cu at (272.0, 20.0)
- added REF**: Choke_LQW2UA_Reflow, Choke_LQW2UA_Reflow, F.Cu at (244.0, 20.0)
- added REF**: Choke_LQW31H_Hand, Choke_LQW31H_Hand, F.Cu at (272.0, 30.0)
- added REF**: Choke_LQB18N_Flow, Choke_LQB18N_Flow, F.Cu at (34.0, 140.0)
- added REF**: Choke_LQW31H_Reflow, Choke_LQW31H_Reflow, F.Cu at (244.0, 30.0)
- added REF**: Choke_LQB18N_Hand, Choke_LQB18N_Hand, F.Cu at (48.0, 140.0)
- added REF**: Choke_LQB18N_Reflow, Choke_LQB18N_Reflow, F.Cu at (20.0, 140.0)
- added REF**: Choke_LQG15H_Hand, Choke_LQG15H_Hand, F.Cu at (48.0, 150.0)
- added REF**: Choke_LQG15H_Reflow, Choke_LQG15H_Reflow, F.Cu at (20.0, 150.0)
- added REF**: Choke_LQG18H_Hand, Choke_LQG18H_Hand, F.Cu at (48.0, 160.0)
- added REF**: CD105, Choke_CD105, F.Cu at (34.0, 30.0)
- added REF**: Choke_LQG18H_Reflow, Choke_LQG18H_Reflow, F.Cu at (20.0, 160.0)
- added REF**: Choke_LQH2HP_GR_Hand, Choke_LQH2HP_GR_Hand, F.Cu at (48.0, 170.0)
- added REF**: Choke_LQH2HP_GR_Reflow, Choke_LQH2HP_GR_Reflow, F.Cu at (20.0, 170.0)
- added REF**: Choke_LQH2HP_Hand, Choke_LQH2HP_Hand, F.Cu at (48.0, 180.0)
- added REF**: Choke_LQH2HP_Reflow, Choke_LQH2HP_Reflow, F.Cu at (20.0, 180.0)
- added REF**: Choke_LQH2MC_Hand, Choke_LQH2MC_Hand, F.Cu at (48.0, 190.0)
- added REF**: Choke_LQH2MC_Reflow, Choke_LQH2MC_Reflow, F.Cu at (20.0, 190.0)
- added REF**: Choke_LQH31C_Hand, Choke_LQH31C_Hand, F.Cu at (104.0, 20.0)
- added REF**: Choke_LQH31C_Reflow, Choke_LQH31C_Reflow, F.Cu at (76.0, 20.0)
- added REF**: Choke_LQH31H_Hand, Choke_LQH31H_Hand, F.Cu at (104.0, 30.0)
- added REF**: CD32, Choke_CD32, F.Cu at (20.0, 40.0)
- added REF**: Choke_LQH31H_Reflow, Choke_LQH31H_Reflow, F.Cu at (76.0, 30.0)
- added REF**: Choke_LQH31M_Hand, Choke_LQH31M_Hand, F.Cu at (104.0, 40.0)
- added REF**: Choke_LQH31M_Reflow, Choke_LQH31M_Reflow, F.Cu at (76.0, 40.0)
- added REF**: Choke_LQH32C_Hand, Choke_LQH32C_Hand, F.Cu at (104.0, 50.0)
- added REF**: Choke_LQH32C_Reflow, Choke_LQH32C_Reflow, F.Cu at (76.0, 50.0)
- added REF**: Choke_LQH32M_Hand, Choke_LQH32M_Hand, F.Cu at (104.0, 60.0)
- added REF**: Choke_LQH32M_Reflow, Choke_LQH32M_Reflow, F.Cu at (76.0, 60.0)
- added REF**: Choke_LQH32P_Hand, Choke_LQH32P_Hand, F.Cu at (104.0, 70.0)
- added REF**: Choke_LQH32P_Reflow, Choke_LQH32P_Reflow, F.Cu at (76.0, 70.0)
- added REF**: Choke_LQH3N_Hand, Choke_LQH3N_Hand, F.Cu at (104.0, 80.0)
- added REF**: CD43, Choke_CD43, F.Cu at (34.0, 50.0)
- added REF**: Choke_LQH3N_Reflow, Choke_LQH3N_Reflow, F.Cu at (76.0, 80.0)
- added REF**: Choke_LQH43C_Hand, Choke_LQH43C_Hand, F.Cu at (104.0, 90.0)
- added REF**: Choke_LQH43C_Reflow, Choke_LQH43C_Reflow, F.Cu at (76.0, 90.0)
- added REF**: Choke_LQH43M_Hand, Choke_LQH43M_Hand, F.Cu at (104.0, 100.0)
- added REF**: Choke_LQH43M_Reflow, Choke_LQH43M_Reflow, F.Cu at (76.0, 100.0)
- added REF**: Choke_LQH43N_Hand, Choke_LQH43N_Hand, F.Cu at (104.0, 110.0)
- added REF**: Choke_LQH43N_Reflow, Choke_LQH43N_Reflow, F.Cu at (76.0, 110.0)
- added REF**: Choke_LQH43P_Hand, Choke_LQH43P_Hand, F.Cu at (104.0, 120.0)
- added REF**: Choke_LQH43P_Reflow, Choke_LQH43P_Reflow, F.Cu at (76.0, 120.0)
- added REF**: Choke_LQH44N_Hand, Choke_LQH44N_Hand, F.Cu at (104.0, 130.0)
- added REF**: CD54, Choke_CD54, F.Cu at (20.0, 60.0)
- added REF**: Choke_LQH44N_Reflow, Choke_LQH44N_Reflow, F.Cu at (76.0, 130.0)
- added REF**: Choke_LQH44P_Hand, Choke_LQH44P_Hand, F.Cu at (104.0, 140.0)
- added REF**: Choke_LQH44P_Reflow, Choke_LQH44P_Reflow, F.Cu at (76.0, 140.0)
- added REF**: Choke_LQH55D_Hand, Choke_LQH55D_Hand, F.Cu at (104.0, 150.0)
- added REF**: Choke_LQH55D_Reflow, Choke_LQH55D_Reflow, F.Cu at (76.0, 150.0)
- added REF**: Choke_LQH5BP_Hand, Choke_LQH5BP_Hand, F.Cu at (104.0, 160.0)
- added REF**: Choke_LQH5BP_Reflow, Choke_LQH5BP_Reflow, F.Cu at (76.0, 160.0)
- added REF**: Choke_LQH66S_Hand, Choke_LQH66S_Hand, F.Cu at (104.0, 170.0)
- added REF**: Choke_LQH66S_Reflow, Choke_LQH66S_Reflow, F.Cu at (76.0, 170.0)
- added REF**: Choke_LQM18F_Flow, Choke_LQM18F_Flow, F.Cu at (90.0, 180.0)
- added REF**: CD73, Choke_CD73, F.Cu at (34.0, 70.0)
- added REF**: Choke_LQM18F_Hand, Choke_LQM18F_Hand, F.Cu at (104.0, 180.0)
- added REF**: Choke_LQM18F_Reflow, Choke_LQM18F_Reflow, F.Cu at (76.0, 180.0)
- added REF**: Choke_LQM18N_Flow, Choke_LQM18N_Flow, F.Cu at (90.0, 190.0)
- added REF**: Choke_LQM18N_Hand, Choke_LQM18N_Hand, F.Cu at (104.0, 190.0)
- added REF**: Choke_LQM18N_Reflow, Choke_LQM18N_Reflow, F.Cu at (76.0, 190.0)
- added REF**: Choke_LQM18P_Flow, Choke_LQM18P_Flow, F.Cu at (146.0, 20.0)
- added REF**: Choke_LQM18P_Hand, Choke_LQM18P_Hand, F.Cu at (160.0, 20.0)
- added REF**: Choke_LQM18P_Reflow, Choke_LQM18P_Reflow, F.Cu at (132.0, 20.0)
- added REF**: Choke_LQM21D_Hand, Choke_LQM21D_Hand, F.Cu at (160.0, 30.0)
- added REF**: Choke_LQM21D_Reflow, Choke_LQM21D_Reflow, F.Cu at (132.0, 30.0)
- added REF**: CD75, Choke_CD75, F.Cu at (20.0, 80.0)
- added REF**: Choke_LQM21F_Hand, Choke_LQM21F_Hand, F.Cu at (160.0, 40.0)
- added REF**: Choke_LQM21F_Reflow, Choke_LQM21F_Reflow, F.Cu at (132.0, 40.0)
- added REF**: Choke_LQM21N_Flow, Choke_LQM21N_Flow, F.Cu at (146.0, 50.0)
- added REF**: Choke_LQM21N_Hand, Choke_LQM21N_Hand, F.Cu at (160.0, 50.0)
- added REF**: Choke_LQM21N_Reflow, Choke_LQM21N_Reflow, F.Cu at (132.0, 50.0)
- added REF**: Choke_LQM21P_Hand, Choke_LQM21P_Hand, F.Cu at (160.0, 60.0)
- added REF**: Choke_LQM21P_Reflow, Choke_LQM21P_Reflow, F.Cu at (132.0, 60.0)
- added REF**: Choke_LQM2HP_GH_1.5A_Hand, Choke_LQM2HP_GH_1.5A_Hand, F.Cu at (160.0, 70.0)
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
